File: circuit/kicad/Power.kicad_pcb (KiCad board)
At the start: 2 copper layers, 67 parts, among them J1 ILG2, J2 PA3, J3 FFC7, J4 FFC4, J5 PA2, J6 PA2, J7 FFC5, Q1 CXDM4060P, SW1 SW_DPDT_x2, SW2 220AMB16R, SW3 SKRPABE010, SW4 SKRPABE010, SW5 SKRPABE010, U1 AZ1117R-5.0TRE1, U2 AZ1117IH-3.3TRG1, U3 DRV8874, U4 DRV8874

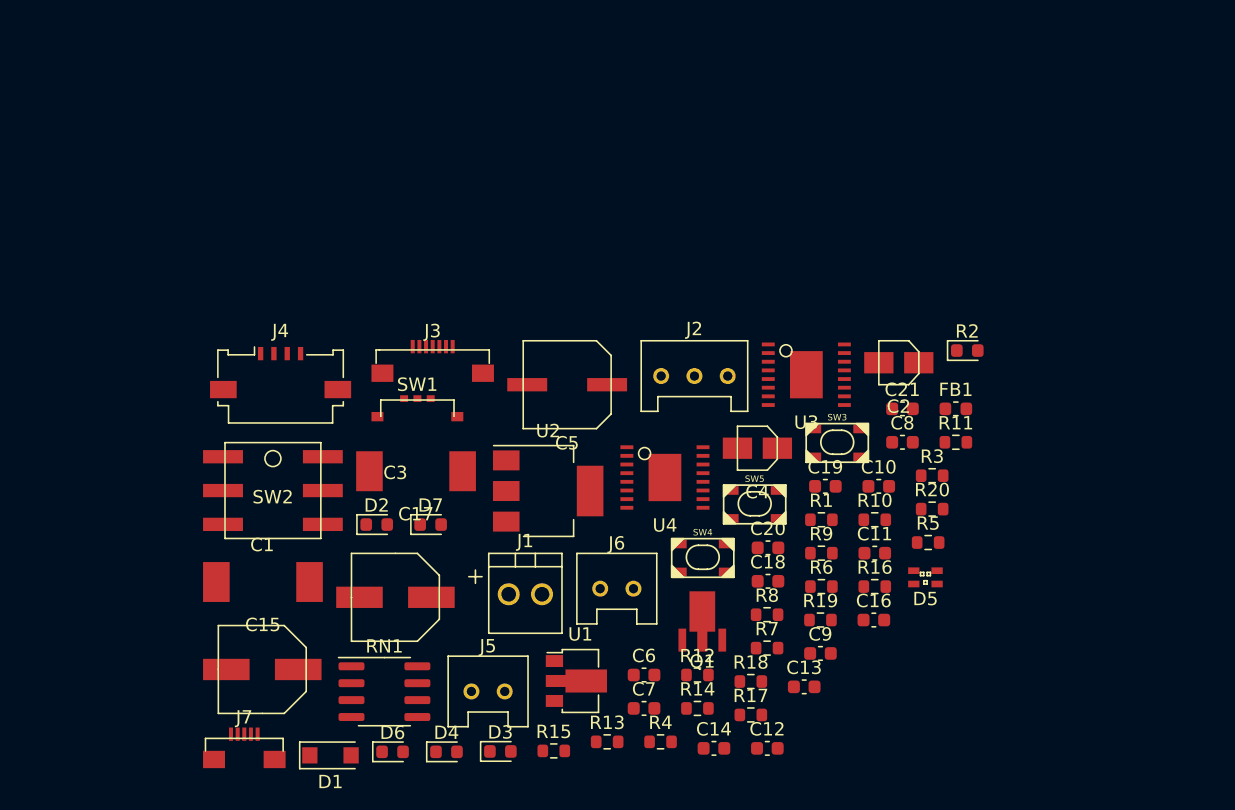
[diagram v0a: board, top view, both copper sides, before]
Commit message: サイドセンサのパターンは完成。メイン基板のフットプリント配置は完了。
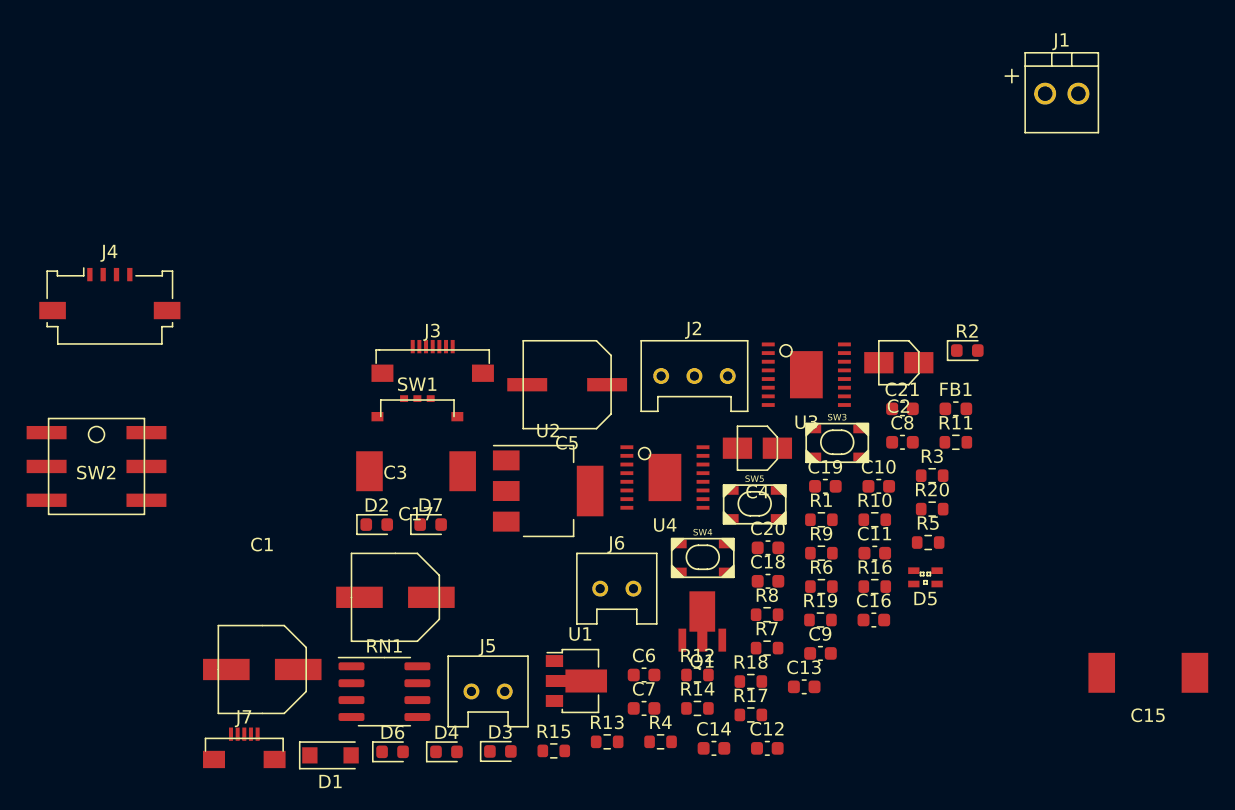
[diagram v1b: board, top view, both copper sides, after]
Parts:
- moved C15 66.8 mm to (197.5, 125.5)
- moved J1 55.1 mm to (191.0, 82.0)
- moved J4 14.1 mm to (119.5, 96.5)
- moved SW2 13.4 mm to (118.5, 110.0)

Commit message: パーツ配置まではとりあえず終わらせた。後は配線すればいい。
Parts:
- removed the J3 at (143.8, 103.0)
- removed J7: FFC5, FFC:Molex_0545480571_01x05_P0.5mm
- added J4: FFC7, Connector_PinHeader_1.00mm:PinHeader_1x12_P1.00mm_Vertical, F.Cu at (-13.0, 23.8)
- C1, C11, C12, C13, C14, C15, C18, C2, C20, C3, C4, C5, C6, D1, FB1, Q1, R1, R13, R15, R20, R5, R6, R7, R8, RN1, U1, U3: moved to B.Cu
- J3: renamed from J4; moved to B.Cu
- R17: value 1.5k -> 1.2k
- R19: value 1.2k -> 1.5k
- moved R11 232.0 mm to (-25.2, 6.00), turned to 270 degrees
- moved D5 230.3 mm to (-21.0, 7.20), turned to 180 degrees
- moved FB1 230.0 mm to (-7.75, -22.8)
- moved R12 228.1 mm to (-30.5, 6.00), turned to 270 degrees
- moved C2 227.9 mm to (-16.2, -15.8), turned to 90 degrees
- moved R3 222.2 mm to (1.40, -19.8), turned to 90 degrees
- moved R4 222.2 mm to (-2.60, -19.8), turned to 90 degrees
- moved C15 220.0 mm to (25.8, -12.0), turned to 180 degrees
- moved U1 218.7 mm to (-11.2, -16.5)
- moved R17 217.9 mm to (-14.2, 8.75), turned to 270 degrees
- moved C6 217.3 mm to (-3.00, -18.5), turned to 90 degrees
- moved J2 217.0 mm to (-22.0, -9.50), turned to 180 degrees
- moved R19 216.9 mm to (-16.2, 15.2), turned to 270 degrees
- moved R2 215.7 mm to (5.40, -19.8), turned to 90 degrees
- moved C10 215.7 mm to (-9.50, 3.60)
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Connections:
- C10 pad 1: /Rotary1 -> /Rotary4
- C7 pad 1: /Rotary8 -> /Rotary1
- C8 pad 1: /Rotary4 -> /Rotary8
- J1 pad 1: (no net) -> GND
- J3 pad 3: /DRV2_EN -> /DRV2_PN
- J3 pad 4: /DRV2_PN -> /DRV2_EN
- R17 pad 1: Net-(D5-Pad4) -> Net-(D5-Pad2)
- R19 pad 1: Net-(D5-Pad2) -> Net-(D5-Pad4)
- RN1 pad 1: /Rotary8 -> /Rotary1
- RN1 pad 2: /Rotary4 -> /Rotary8
- RN1 pad 4: /Rotary1 -> /Rotary4
- SW1 pad 1: (no net) -> GND
- U4 pad 10: Net-(J6-Pad1) -> Net-(J6-Pad2)
- U4 pad 8: Net-(J6-Pad2) -> Net-(J6-Pad1)
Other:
- board outline added: 78.8 x 54.8 mm

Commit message: hoge
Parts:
- C8, C9: moved to B.Cu
- J4: footprint Connector_PinHeader_1.00mm:PinHeader_1x12_P1.00mm_Vertical -> FFC:WürthElektronik_687112183722_01x12_P0.5mm
- R1: moved to F.Cu
- moved U4 8.00 mm to (5.25, 2.00)
- moved J6 7.25 mm to (12.5, 2.00)
- moved J4 7.02 mm to (-19.8, 25.5), turned to 0 degrees
- moved J1 6.40 mm to (25.0, -23.0)
- moved R10 5.25 mm to (4.50, 9.75)
- moved R14 5.25 mm to (6.00, 8.75)
- moved R16 5.25 mm to (7.50, 8.75)
- moved R9 5.25 mm to (3.00, 9.75)
- moved R1 5.00 mm to (18.0, -23.0), turned to 180 degrees
- moved R13 2.50 mm to (26.8, 9.75)
- moved R15 2.50 mm to (23.8, 8.75)
- moved R20 2.50 mm to (25.2, 8.75)
- moved R8 2.50 mm to (28.2, 9.75)
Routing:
- net /DRV2_EN: track 0.00 -> 20.3 mm, vias 0 -> 1
- net /DRV2_PN: track 0.00 -> 19.6 mm, vias 0 -> 1
- net /Rotary2: track 0.00 -> 16.7 mm, vias 0 -> 2
- net /DRV1_PN: track 0.00 -> 15.9 mm, vias 0 -> 2
- net /DRV1_EN: track 0.00 -> 15.8 mm, vias 0 -> 2
- net +5V: track 0.00 -> 15.5 mm
- net /Rotary4: track 0.00 -> 14.3 mm, vias 0 -> 1
- net /Rotary1: track 0.00 -> 14.3 mm, vias 0 -> 1
- net Net-(Q1-Pad1): track 0.00 -> 12.0 mm, vias 0 -> 1
- net /Rotary8: track 0.00 -> 10.9 mm, vias 0 -> 2
- net Net-(D5-Pad4): track 0.00 -> 9.05 mm
- net /SW3: track 0.00 -> 7.65 mm, vias 0 -> 1
- net /SW1: track 0.00 -> 7.60 mm, vias 0 -> 1
- net Net-(D5-Pad2): track 0.00 -> 6.38 mm
- net Net-(D5-Pad3): track 0.00 -> 6.31 mm
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
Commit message: とりあえず完成
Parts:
- C21: moved to B.Cu
- J3, Q1: moved to F.Cu
- SW1: footprint Switch:SSAJ120100 -> Switch:SSSS810701
- moved C3 12.8 mm to (13.4, -21.1), turned to 270 degrees
- moved C16 10.6 mm to (3.60, -10.2)
- moved C19 10.6 mm to (3.60, -7.80)
- moved C21 8.00 mm to (3.00, -3.60), turned to 270 degrees
- moved Q1 7.94 mm to (16.4, -15.3), turned to 180 degrees
- moved J4 6.16 mm to (-25.8, 24.1)
- moved SW1 5.58 mm to (18.4, -24.6)
- moved C17 5.35 mm to (16.4, -7.10), turned to 90 degrees
- moved R19 5.08 mm to (-17.8, 10.4)
- moved R1 4.31 mm to (16.4, -19.0)
- moved J1 3.45 mm to (26.3, -19.8)
- moved C15 3.05 mm to (28.8, -12.0)
- moved J3 3.00 mm to (18.0, 19.5), turned to 0 degrees
- moved R18 2.51 mm to (-16.0, 9.60)
- moved D2 0.14 mm to (5.30, -23.7)
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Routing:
- net +3V3: track 0.00 -> 96.7 mm, vias 0 -> 2
- net +5V: track 15.5 -> 108.1 mm, vias 0 -> 2
- net +BATT: track 3.79 -> 77.3 mm, vias 1 -> 6
- net GND: track 0.00 -> 70.1 mm, vias 0 -> 41
- net Net-(J6-Pad2): track 0.00 -> 35.9 mm
- net /SW3: track 7.65 -> 42.2 mm
- net /SW2: track 3.13 -> 37.1 mm, vias 0 -> 1
- net /Rotary8: track 10.9 -> 43.7 mm, vias 2 -> 3
- net /SW1: track 7.60 -> 35.3 mm
- net /Rotary1: track 14.3 -> 39.9 mm, vias 1 -> 2
- net /Rotary2: track 16.7 -> 36.4 mm
- net Net-(J4-Pad5): track 0.00 -> 19.4 mm
- net Net-(J4-Pad4): track 0.00 -> 18.0 mm
- net Net-(J4-Pad3): track 0.00 -> 16.0 mm
- net /Rotary4: track 14.3 -> 29.6 mm
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- added copper zone on B.Cu, net GND
- added copper zone on F.Cu, net GND

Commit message: 点検
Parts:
- C14, C15, C18, R13, R15, R20, R8, U3: moved to F.Cu
- moved J2 11.0 mm to (-24.6, -20.1), turned to 0 degrees
- moved J5 10.0 mm to (30.8, 1.50), turned to 270 degrees
- moved C20 9.99 mm to (18.8, -1.00)
- moved C16 4.70 mm to (3.60, -5.50)
- moved C14 4.67 mm to (21.8, -5.50), turned to 180 degrees
- moved R15 4.50 mm to (28.2, 8.75)
- moved R8 4.50 mm to (23.8, 9.75)
- moved C18 4.43 mm to (21.8, -4.00), turned to 180 degrees
- moved C19 3.80 mm to (3.60, -4.00)
- moved C21 3.61 mm to (0.50, -1.00), turned to 0 degrees
- moved U3 2.75 mm to (23.5, 2.00)
- moved R13 1.50 mm to (25.2, 9.75)
- moved R20 1.50 mm to (26.8, 8.75)
- moved C17 1.08 mm to (15.5, -6.50)
- moved C15 1.00 mm to (28.8, -13.0)
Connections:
- J3 pad MP: (no net) -> GND
- J4 pad MP: (no net) -> GND
- U3 pad 10: Net-(J5-Pad1) -> Net-(J5-Pad2)
- U3 pad 8: Net-(J5-Pad2) -> Net-(J5-Pad1)
- U3 pad ThermalPad: (no net) -> GND
- U4 pad ThermalPad: (no net) -> GND
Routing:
- net +5V: track 108.1 -> 84.3 mm
- net Net-(J6-Pad2): track 35.9 -> 16.7 mm
- net GND: track 70.1 -> 54.2 mm, vias 41 -> 65
- net +BATT: track 77.3 -> 92.9 mm, vias 6 -> 2
- net Net-(J5-Pad2): track 6.98 -> 17.9 mm
- net /DRV1_EN: track 26.1 -> 15.7 mm, vias 3 -> 0
- net +3V3: track 96.7 -> 104.1 mm, vias 2 -> 4
- net /DRV1_PN: track 21.7 -> 15.5 mm, vias 3 -> 0
- net /DRV2_EN: track 34.9 -> 28.9 mm
- net Net-(C20-Pad1): track 3.17 -> 7.74 mm, vias 0 -> 1
- net Net-(C19-Pad2): track 8.61 -> 4.38 mm
- net Net-(C21-Pad1): track 4.59 -> 7.74 mm
- net Net-(J5-Pad1): track 12.5 -> 9.39 mm
- net Net-(R15-Pad1): track 3.70 -> 5.70 mm
- net Net-(C21-Pad2): track 2.66 -> 4.54 mm
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- added copper zone on F.Cu, net +BATT
- added copper zone on F.Cu, net Net-(J5-Pad2)
- added copper zone on F.Cu, net Net-(J6-Pad2)
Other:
- outline, holes or cut-outs redrawn

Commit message: hoge
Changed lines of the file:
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@@
   (general
     (thickness 1.6)
-    (drawings 24)
-    (tracks 505)
+    (drawings 23)
+    (tracks 504)
     (zones 0)
     (modules 66)
@@
       (net 2 GND))
   )
+  (dimension 15.4 (width 0.15) (layer Dwgs.User)
+    (gr_text "15.400 mm" (at -43 19.7 90) (layer Dwgs.User)
+      (effects (font (size 1 1) (thickness 0.15)))
+    )
+    (feature1 (pts (xy -39.7 12) (xy -42.286421 12)))
+    (feature2 (pts (xy -39.7 27.4) (xy -42.286421 27.4)))
+    (crossbar (pts (xy -41.7 27.4) (xy -41.7 12)))
+    (arrow1a (pts (xy -41.7 12) (xy -41.113579 13.126504)))
+    (arrow1b (pts (xy -41.7 12) (xy -42.286421 13.126504)))
+    (arrow2a (pts (xy -41.7 27.4) (xy -41.113579 26.273496)))
+    (arrow2b (pts (xy -41.7 27.4) (xy -42.286421 26.273496)))
+  )
+  (dimension 78.799998 (width 0.15) (layer Dwgs.User)
+    (gr_text "78.800 mm" (at 0 31.399999 7.271038194e-07) (layer Dwgs.User)
+      (effects (font (size 1 1) (thickness 0.15)))
+    )
+    (feature1 (pts (xy 39.399999 27.399999) (xy 39.399999 30.68642)))
+    (feature2 (pts (xy -39.399999 27.4) (xy -39.399999 30.686421)))
+    (crossbar (pts (xy -39.399999 30.1) (xy 39.399999 30.099999)))
+    (arrow1a (pts (xy 39.399999 30.099999) (xy 38.273495 30.68642)))
+    (arrow1b (pts (xy 39.399999 30.099999) (xy 38.273495 29.513578)))
+    (arrow2a (pts (xy -39.399999 30.1) (xy -38.273495 30.686421)))
+    (arrow2b (pts (xy -39.399999 30.1) (xy -38.273495 29.513579)))
+  )
+  (dimension 54.799999 (width 0.15) (layer Dwgs.User)
+    (gr_text "54.800 mm" (at -47.45 0 90) (layer Dwgs.User)
+      (effects (font (size 1 1) (thickness 0.15)))
+    )
+    (feature1 (pts (xy -39.399999 -27.399999) (xy -46.736421 -27.399999)))
+    (feature2 (pts (xy -39.399999 27.4) (xy -46.736421 27.4)))
+    (crossbar (pts (xy -46.15 27.4) (xy -46.15 -27.399999)))
+    (arrow1a (pts (xy -46.15 -27.399999) (xy -45.563579 -26.273495)))
+    (arrow1b (pts (xy -46.15 -27.399999) (xy -46.736421 -26.273495)))
+    (arrow2a (pts (xy -46.15 27.4) (xy -45.563579 26.273496)))
+    (arrow2b (pts (xy -46.15 27.4) (xy -46.736421 26.273496)))
+  )
   (gr_line (start -21.4 -10.65) (end -21.4 -4.15) (layer Edge.Cuts) (width 0.2))
   (gr_line (start -30.4 -10.65) (end -21.4 -10.65) (layer Edge.Cuts) (width 0.2))
   (gr_line (start -30.4 -4.15) (end -30.4 -10.65) (layer Edge.Cuts) (width 0.2))
   (gr_line (start -21.4 -4.15) (end -30.4 -4.15) (layer Edge.Cuts) (width 0.2))
-  (gr_line (start -3 22) (end -40 22) (layer Dwgs.User) (width 0.15))
-  (gr_line (start -3 28) (end -3 22) (layer Dwgs.User) (width 0.15))
-  (gr_line (start 3 22) (end 3 28) (layer Dwgs.User) (width 0.15))
-  (gr_line (start 3 22) (end 40 22) (layer Dwgs.User) (width 0.15))
   (gr_circle (center -37.15 14.45) (end -35.95 14.45) (layer Edge.Cuts) (width 0.2))
   (gr_circle (center -37.15 -20.449999) (end -35.95 -20.449999) (layer Edge.Cuts) (width 0.2))
@@
   (segment (start -19.15 -17.15) (end -22.1 -20.1) (width 1) (layer B.Cu) (net 3))
   (segment (start -16.35 -17.15) (end -19.15 -17.15) (width 1) (layer B.Cu) (net 3))
-  (segment (start -20.15 -16.15) (end -19.15 -17.15) (width 0.3) (layer B.Cu) (net 3))
-  (segment (start -20.15 -13.4) (end -20.15 -13.4) (width 0.3) (layer B.Cu) (net 3))
-  (segment (start -20.15 -13.4) (end -20.15 -16.15) (width 0.3) (layer B.Cu) (net 3))
-  (via (at -20.15 -13.4) (size 0.8) (drill 0.4) (layers F.Cu B.Cu) (net 3))
   (segment (start -22.975 5.175) (end -23.4 5.175) (width 0.3) (layer F.Cu) (net 3))
-  (segment (start -18.65 -11.9) (end -18.65 0.85) (width 0.3) (layer F.Cu) (net 3))
+  (segment (start -18.65 -11.9) (end -18.65 -11.9) (width 0.3) (layer F.Cu) (net 3))
   (segment (start -18.65 0.85) (end -22.975 5.175) (width 0.3) (layer F.Cu) (net 3))
-  (segment (start -20.15 -13.4) (end -18.65 -11.9) (width 0.3) (layer F.Cu) (net 3))
+  (segment (start -18.65 -11.9) (end -18.65 0.85) (width 0.3) (layer F.Cu) (net 3))
+  (via (at -18.65 -11.9) (size 0.8) (drill 0.4) (layers F.Cu B.Cu) (net 3))
+  (segment (start -18.65 -14.85) (end -16.35 -17.15) (width 0.3) (layer B.Cu) (net 3))
+  (segment (start -18.65 -11.9) (end -18.65 -14.85) (width 0.3) (layer B.Cu) (net 3))
   (segment (start 1.97499 10.19999) (end 2.775 11) (width 0.25) (layer B.Cu) (net 4))
   (segment (start -1.025 11) (end -0.22499 10.19999) (width 0.25) (layer B.Cu) (net 4))
@@
       )
     )
+  )
+  (zone (net 0) (net_name "") (layer B.Cu) (hatch edge 0.508)
+    (connect_pads (clearance 0.508))
+    (min_thickness 0.254)
+    (keepout (tracks allowed) (vias allowed) (copperpour not_allowed))
+    (fill (arc_segments 32) (thermal_gap 0.508) (thermal_bridge_width 0.508))
+    (polygon
+      (pts
+        (xy -18.275 -14.9) (xy -20.525 -17.15) (xy -18.15 -17.15)
+      )
+    )

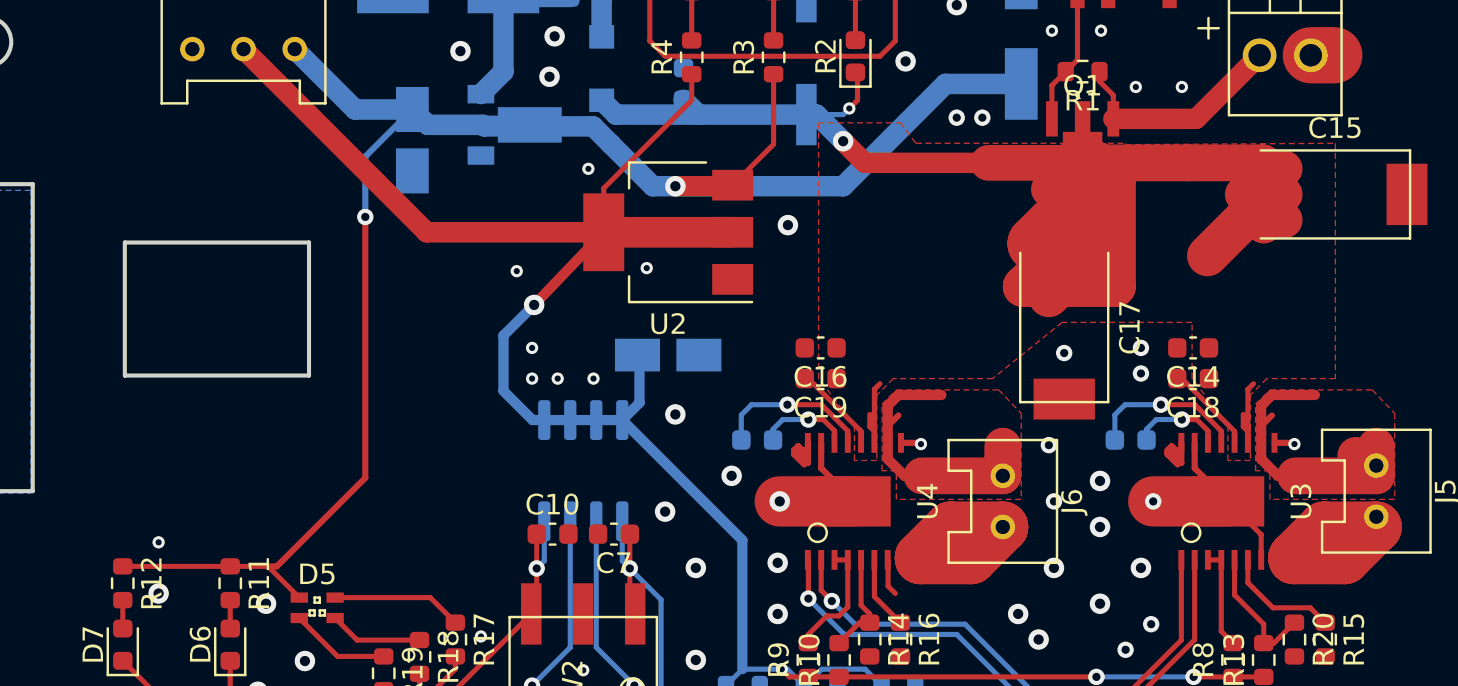
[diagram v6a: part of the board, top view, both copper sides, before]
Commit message: あとはシルクを見やすい位置にもっていくだけ。
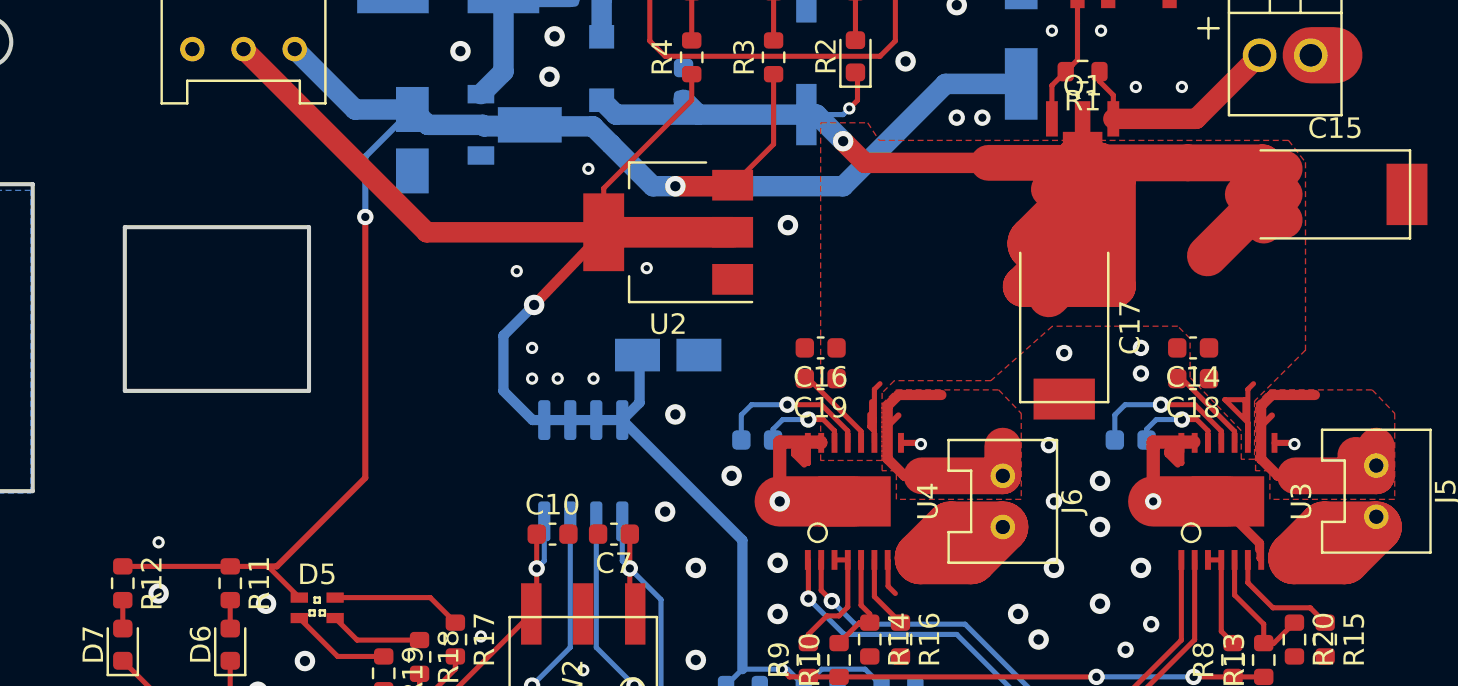
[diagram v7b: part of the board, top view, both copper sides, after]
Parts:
- R17: value 1.2k -> 1.5k
- R19: value 1.5k -> 1.2k
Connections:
- J3 pad MP: GND -> (no net)
- J4 pad MP: GND -> (no net)
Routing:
- net +BATT: track 92.9 -> 97.3 mm
- net GND: track 54.2 -> 57.0 mm
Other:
- outline, holes or cut-outs redrawn
- board text added: "B"
- board text added: "G"
- board text added: "R"

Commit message: これから gerber ファイルを吐き出して先輩たちに見てもらう
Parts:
- moved J5 0.50 mm to (30.8, 2.00)
